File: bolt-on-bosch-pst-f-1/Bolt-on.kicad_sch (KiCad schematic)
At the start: 10 parts

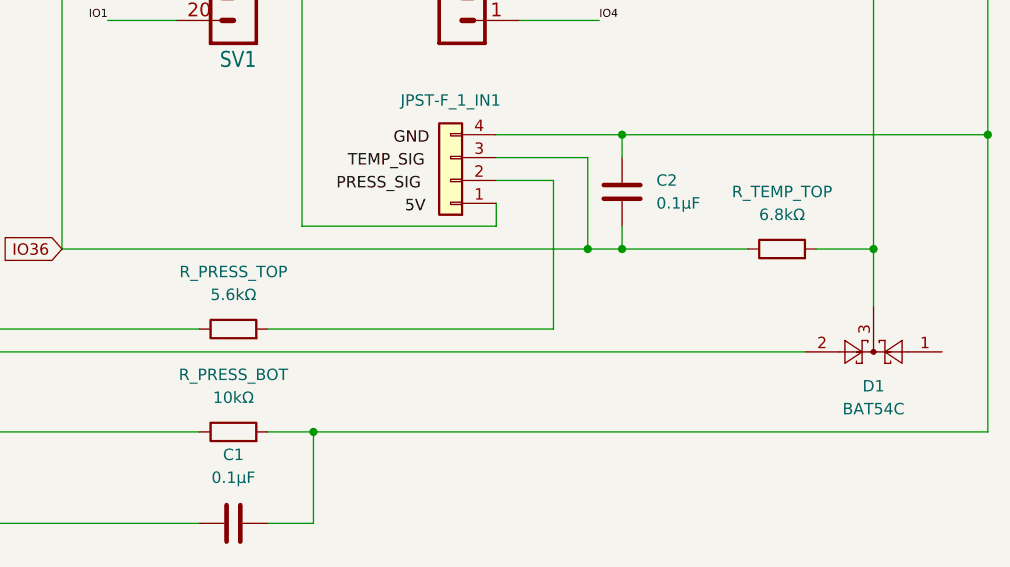
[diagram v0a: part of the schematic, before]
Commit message: fixed resistors name
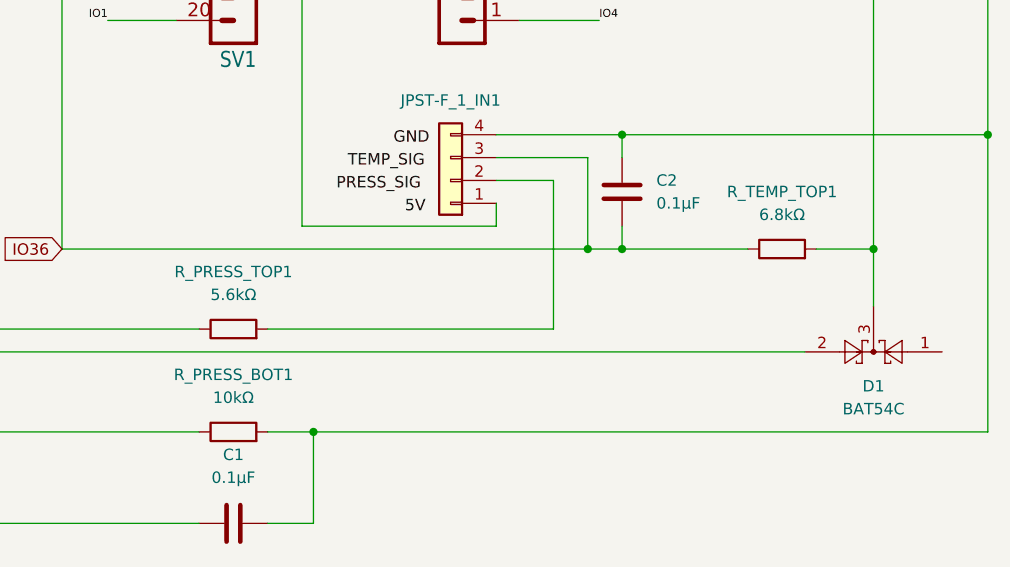
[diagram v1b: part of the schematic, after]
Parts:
- renumbered R_PRESS_BOT to R_PRESS_BOT1, R_PRESS_TOP to R_PRESS_TOP1, R_TEMP_TOP to R_TEMP_TOP1
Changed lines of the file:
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@@
 		(on_board yes)
 		(dnp no)
-		(property "Reference" "R_PRESS_TOP"
+		(property "Reference" "R_PRESS_TOP1"
 			(at 199.39 201.93 90)
 			(effects
@@
 			(project ""
 				(path "/d642a88c-4bf2-433d-8cf9-b5aeaa3805cb"
-					(reference "R_PRESS_TOP")
+					(reference "R_PRESS_TOP1")
 					(unit 1)
 				)
@@
 		(dnp no)
 		(fields_autoplaced yes)
-		(property "Reference" "R_TEMP_TOP"
+		(property "Reference" "R_TEMP_TOP1"
 			(at 260.35 193.04 90)
 			(effects
@@
 			(project "Bolt-on"
 				(path "/d642a88c-4bf2-433d-8cf9-b5aeaa3805cb"
-					(reference "R_TEMP_TOP")
+					(reference "R_TEMP_TOP1")
 					(unit 1)
 				)
@@
 		(dnp no)
 		(fields_autoplaced yes)
-		(property "Reference" "R_PRESS_BOT"
+		(property "Reference" "R_PRESS_BOT1"
 			(at 199.39 213.36 90)
 			(effects
@@
 			(project "Bolt-on"
 				(path "/d642a88c-4bf2-433d-8cf9-b5aeaa3805cb"
-					(reference "R_PRESS_BOT")
-					(unit 1)
-				)
+					(reference "R_PRESS_BOT1")
+					(unit 1)
+				)

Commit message: cleanup kicad design
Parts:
- renumbered R_PRESS_BOT1 to R_PRESS_BOT, R_PRESS_TOP1 to R_PRESS_TOP, R_TEMP_TOP1 to R_TEMP_TOP
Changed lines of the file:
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@@
 		(on_board yes)
 		(dnp no)
-		(property "Reference" "R_PRESS_TOP1"
+		(property "Reference" "R_PRESS_TOP"
 			(at 199.39 201.93 90)
 			(effects
@@
 			(project ""
 				(path "/d642a88c-4bf2-433d-8cf9-b5aeaa3805cb"
-					(reference "R_PRESS_TOP1")
+					(reference "R_PRESS_TOP")
 					(unit 1)
 				)
@@
 		(dnp no)
 		(fields_autoplaced yes)
-		(property "Reference" "R_TEMP_TOP1"
+		(property "Reference" "R_TEMP_TOP"
 			(at 260.35 193.04 90)
 			(effects
@@
 			(project "Bolt-on"
 				(path "/d642a88c-4bf2-433d-8cf9-b5aeaa3805cb"
-					(reference "R_TEMP_TOP1")
+					(reference "R_TEMP_TOP")
 					(unit 1)
 				)
@@
 		(dnp no)
 		(fields_autoplaced yes)
-		(property "Reference" "R_PRESS_BOT1"
+		(property "Reference" "R_PRESS_BOT"
 			(at 199.39 213.36 90)
 			(effects
@@
 			(project "Bolt-on"
 				(path "/d642a88c-4bf2-433d-8cf9-b5aeaa3805cb"
-					(reference "R_PRESS_BOT1")
-					(unit 1)
-				)
+					(reference "R_PRESS_BOT")
+					(unit 1)
+				)
